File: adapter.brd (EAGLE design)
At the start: 11.3 x 34.7 mm, 14 parts

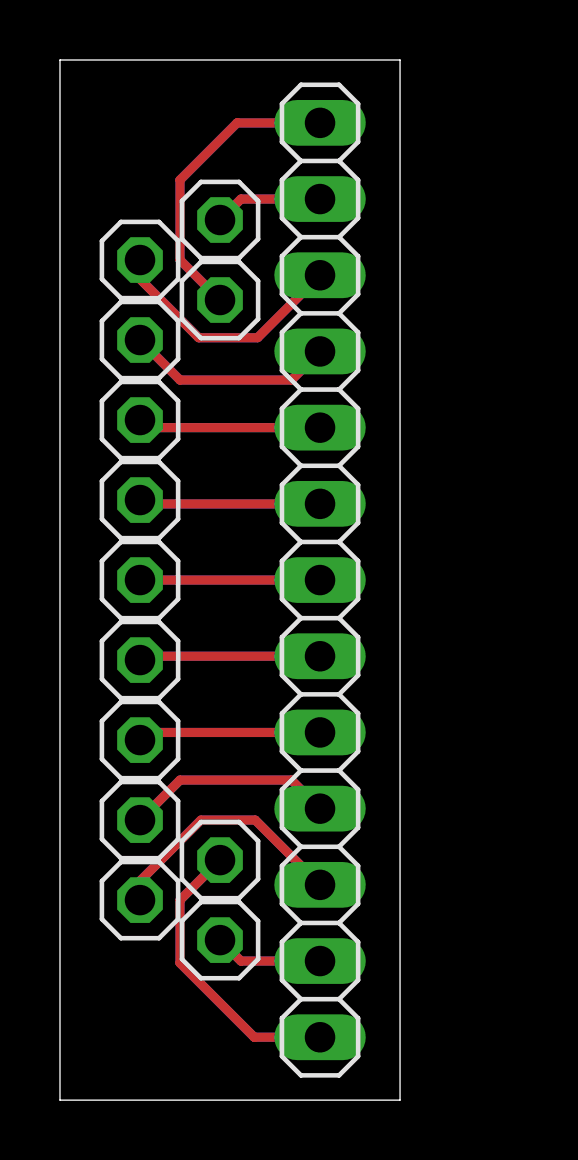
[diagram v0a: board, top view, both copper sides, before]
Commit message: update adapter board for SMD
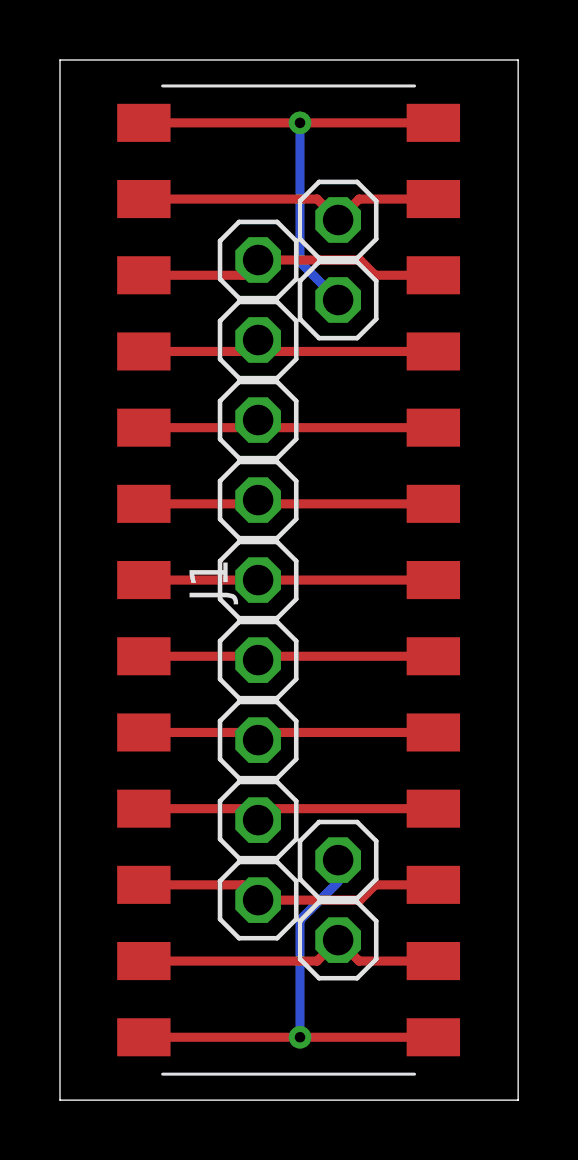
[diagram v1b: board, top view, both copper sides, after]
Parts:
- removed JP1: (no value), pinhead:1X13
- added J1: 71607-313LF, ltobms:71607313LF
- moved JP13 3.94 mm to (9.27, 29.3)
- moved JP14 3.94 mm to (9.27, 26.7)
- moved JP2 3.94 mm to (9.27, 8.00)
- moved JP3 3.94 mm to (9.27, 5.33)
- moved JP10 3.94 mm to (6.60, 22.7)
- moved JP11 3.94 mm to (6.60, 25.3)
- moved JP12 3.94 mm to (6.60, 28.0)
- moved JP4 3.94 mm to (6.60, 6.67)
- moved JP5 3.94 mm to (6.60, 9.33)
- moved JP6 3.94 mm to (6.60, 12.0)
- moved JP7 3.94 mm to (6.60, 14.7)
- moved JP8 3.94 mm to (6.60, 17.3)
- moved JP9 3.94 mm to (6.60, 20.0)
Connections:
- net N$1: now also J1.1, J1.26; no longer JP1.1
- net N$10: now also J1.10, J1.17; no longer JP1.10
- net N$11: now also J1.11, J1.16; no longer JP1.11
- net N$12: now also J1.12, J1.15; no longer JP1.12
- net N$13: now also J1.13, J1.14; no longer JP1.13
- net N$2: now also J1.2, J1.25; no longer JP1.2
- net N$3: now also J1.24, J1.3; no longer JP1.3
- net N$4: now also J1.23, J1.4; no longer JP1.4
- net N$5: now also J1.22, J1.5; no longer JP1.5
- net N$6: now also J1.21, J1.6; no longer JP1.6
- net N$7: now also J1.20, J1.7; no longer JP1.7
- net N$8: now also J1.19, J1.8; no longer JP1.8
- net N$9: now also J1.18, J1.9; no longer JP1.9
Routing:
- net N$26: track 10.0 -> 0.00 mm
- net N$14: track 9.67 -> 0.00 mm
- net N$16: track 8.37 -> 0.00 mm
- net N$24: track 8.31 -> 0.00 mm
- net N$23: track 6.95 -> 0.00 mm
- net N$17: track 6.95 -> 0.00 mm
- net N$2: track 3.62 -> 10.2 mm
- net N$12: track 3.62 -> 10.2 mm
- net N$1: track 9.67 -> 16.1 mm, vias 0 -> 1
- net N$18: track 6.11 -> 0.00 mm
- net N$22: track 6.11 -> 0.00 mm
- net N$13: track 10.0 -> 16.1 mm, vias 0 -> 1
- net N$21: track 6.05 -> 0.00 mm
- net N$19: track 6.05 -> 0.00 mm
- net N$20: track 6.00 -> 0.00 mm
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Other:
- board size 11.3 x 34.7 mm -> 15.3 x 34.7 mm

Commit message: add labels
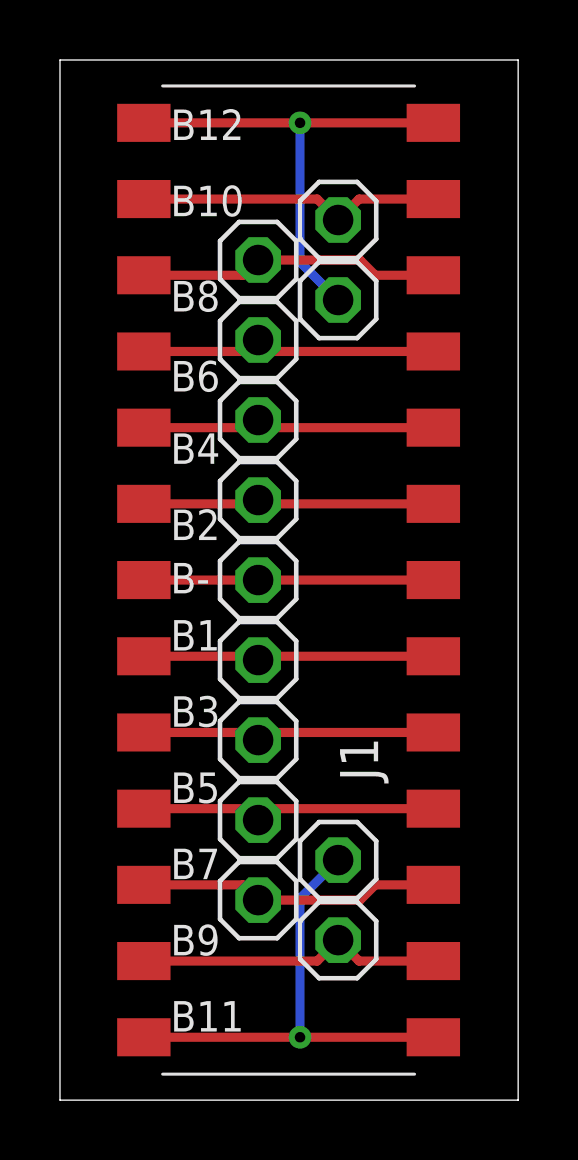
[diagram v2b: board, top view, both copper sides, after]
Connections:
- net N$1 renamed B11
- net N$10 renamed B6
- net N$11 renamed B8
- net N$12 renamed B10
- net N$13 renamed B12
- net N$2 renamed B9
- net N$3 renamed B7
- net N$4 renamed B5
- net N$5 renamed B3
- net N$6 renamed B1
- net N$7 renamed B-
- net N$8 renamed B2
- net N$9 renamed B4
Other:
- board text added: "B-"
- board text added: "B1"
- board text added: "B10"
- board text added: "B11"
- board text added: "B12"
- board text added: "B2"
- board text added: "B3"
- board text added: "B4"
- board text added: "B5"
- board text added: "B6"
- board text added: "B7"
- board text added: "B8"
- board text added: "B9"
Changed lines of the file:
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@@
 <wire x1="0" y1="34.671" x2="0" y2="0" width="0" layer="20"/>
 <dimension x1="15.27175" y1="34.671" x2="0" y2="34.671" x3="7.635875" y3="36.0045" textsize="1.778" layer="1" unit="inch"/>
+<text x="3.683" y="32.004" size="1.016" layer="25">B12</text>
+<text x="3.683" y="29.464" size="1.016" layer="25">B10</text>
+<text x="3.683" y="26.289" size="1.016" layer="25">B8</text>
+<text x="3.683" y="23.622" size="1.016" layer="25">B6</text>
+<text x="3.683" y="21.209" size="1.016" layer="25">B4</text>
+<text x="3.683" y="18.669" size="1.016" layer="25">B2</text>
+<text x="3.683" y="16.891" size="1.016" layer="25">B-</text>
+<text x="3.683" y="14.986" size="1.016" layer="25">B1</text>
+<text x="3.683" y="12.446" size="1.016" layer="25">B3</text>
+<text x="3.683" y="9.906" size="1.016" layer="25">B5</text>
+<text x="3.683" y="7.366" size="1.016" layer="25">B7</text>
+<text x="3.683" y="4.826" size="1.016" layer="25">B9</text>
+<text x="3.683" y="2.286" size="1.016" layer="25">B11</text>
 </plain>
 <attributes>
@@
 <attribute name="MOUSER_PART_NUMBER" value="649-71607-313LF" x="7.62" y="17.3355" size="1.778" layer="27" rot="R90" display="off"/>
 <attribute name="MOUSER_PRICE-STOCK" value="https://www.mouser.co.uk/ProductDetail/Amphenol-FCI/71607-313LF?qs=yJYkLTYh574OxHiM9YZfow%3D%3D" x="7.62" y="17.3355" size="1.778" layer="27" rot="R90" display="off"/>
-<attribute name="NAME" x="4.953" y="17.3355" size="1.27" layer="25" rot="R90" align="center"/>
-<attribute name="VALUE" x="9.62025" y="17.3355" size="1.27" layer="27" rot="R90" align="center"/>
+<attribute name="NAME" x="9.9695" y="11.3665" size="1.27" layer="25" rot="R90" align="center"/>
+<attribute name="VALUE" x="10.00125" y="18.669" size="1.27" layer="27" rot="R90" align="center"/>
 </element>
 </elements>
 <signals>
-<signal name="N$1" class="1">
+<signal name="B11" class="1">
 <contactref element="JP2" pad="1"/>
 <contactref element="J1" pad="26"/>
@@
 <wire x1="2.795" y1="2.0955" x2="8.001" y2="2.0955" width="0.3048" layer="1"/>
 <wire x1="8.001" y1="2.0955" x2="12.445" y2="2.0955" width="0.3048" layer="1"/>
-<wire x1="9.271" y1="8.001" x2="9.271" y2="7.27075" width="0.3048" layer="16"/>
-<wire x1="9.271" y1="7.27075" x2="8.001" y2="6.00075" width="0.3048" layer="16"/>
-<wire x1="8.001" y1="6.00075" x2="8.001" y2="2.0955" width="0.3048" layer="16"/>
 <via x="8.001" y="2.0955" extent="1-16" drill="0.35"/>
-</signal>
-<signal name="N$2" class="1">
+<wire x1="9.271" y1="8.001" x2="8.001" y2="6.731" width="0.3048" layer="16"/>
+<wire x1="8.001" y1="6.731" x2="8.001" y2="2.0955" width="0.3048" layer="16"/>
+</signal>
+<signal name="B9" class="1">
 <contactref element="JP3" pad="1"/>
 <contactref element="J1" pad="25"/>
@@
 <wire x1="9.9695" y1="4.6355" x2="9.271" y2="5.334" width="0.3048" layer="1"/>
 </signal>
-<signal name="N$3" class="1">
+<signal name="B7" class="1">
 <contactref element="JP4" pad="1"/>
 <contactref element="J1" pad="24"/>
@@
 <wire x1="6.096" y1="7.1755" x2="6.604" y2="6.6675" width="0.3048" layer="1"/>
 </signal>
-<signal name="N$4" class="1">
+<signal name="B5" class="1">
 <contactref element="JP5" pad="1"/>
 <contactref element="J1" pad="23"/>
@@
 <wire x1="6.985" y1="9.7155" x2="6.604" y2="9.3345" width="0.3048" layer="1"/>
 </signal>
-<signal name="N$5" class="1">
+<signal name="B3" class="1">
 <contactref element="JP6" pad="1"/>
 <contactref element="J1" pad="22"/>
@@
 <wire x1="6.858" y1="12.2555" x2="6.604" y2="12.0015" width="0.3048" layer="1"/>
 </signal>
-<signal name="N$6" class="1">
+<signal name="B1" class="1">
 <contactref element="JP7" pad="1"/>
 <contactref element="J1" pad="21"/>
@@
 <wire x1="6.731" y1="14.7955" x2="6.604" y2="14.6685" width="0.3048" layer="1"/>
 </signal>
-<signal name="N$7" class="1">
+<signal name="B-" class="1">
 <contactref element="JP8" pad="1"/>
 <contactref element="J1" pad="20"/>
@@
 <wire x1="12.445" y1="17.3355" x2="6.604" y2="17.3355" width="0.3048" layer="1"/>
 </signal>
-<signal name="N$8" class="1">
+<signal name="B2" class="1">
 <contactref element="JP9" pad="1"/>
 <contactref element="J1" pad="19"/>
@@
 <wire x1="6.731" y1="19.8755" x2="6.604" y2="20.0025" width="0.3048" layer="1"/>
 </signal>
-<signal name="N$9" class="1">
+<signal name="B4" class="1">
 <contactref element="JP10" pad="1"/>
 <contactref element="J1" pad="18"/>
@@
 <wire x1="6.858" y1="22.4155" x2="6.604" y2="22.6695" width="0.3048" layer="1"/>
 </signal>
-<signal name="N$10" class="1">
+<signal name="B6" class="1">
 <contactref element="JP11" pad="1"/>
 <contactref element="J1" pad="17"/>
@@
 <wire x1="6.985" y1="24.9555" x2="6.604" y2="25.3365" width="0.3048" layer="1"/>
 </signal>
-<signal name="N$11" class="1">
+<signal name="B8" class="1">
 <contactref element="JP12" pad="1"/>
 <contactref element="J1" pad="16"/>
@@
 <wire x1="10.00125" y1="28.0035" x2="6.604" y2="28.0035" width="0.3048" layer="1"/>
 </signal>
-<signal name="N$12" class="1">
+<signal name="B10" class="1">
 <contactref element="JP13" pad="1"/>
 <contactref element="J1" pad="15"/>
@@
 <wire x1="9.9695" y1="30.0355" x2="9.271" y2="29.337" width="0.3048" layer="1"/>
 </signal>
-<signal name="N$13" class="1">
+<signal name="B12" class="1">
 <contactref element="JP14" pad="1"/>
 <contactref element="J1" pad="14"/>
